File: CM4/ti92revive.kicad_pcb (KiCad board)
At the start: 2 copper layers, 205 x 116.7 mm, 175 parts, among them J1 USB_B, J2 Conn_01x02, J3 Conn_01x02, J4 USB_A, J5 USB_A, Q1 EMH3, U1 Compute_Module_4_Connectors, U2 NCP114ASN330T1G, U3 BQ25887RGET, U4 MAX17643, U5 ATTINY85-20PU, U6 TQ2SA-L2-3V-Z-Remake, U7 TUSB4041I, U8 TLV740P, U9 SK5126, Y1 24 MHz

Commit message: Cleaned Up the Matrix contolller
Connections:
- net FB renamed /PowerSupply/FB
- U9 pad 49: (no net) -> GND

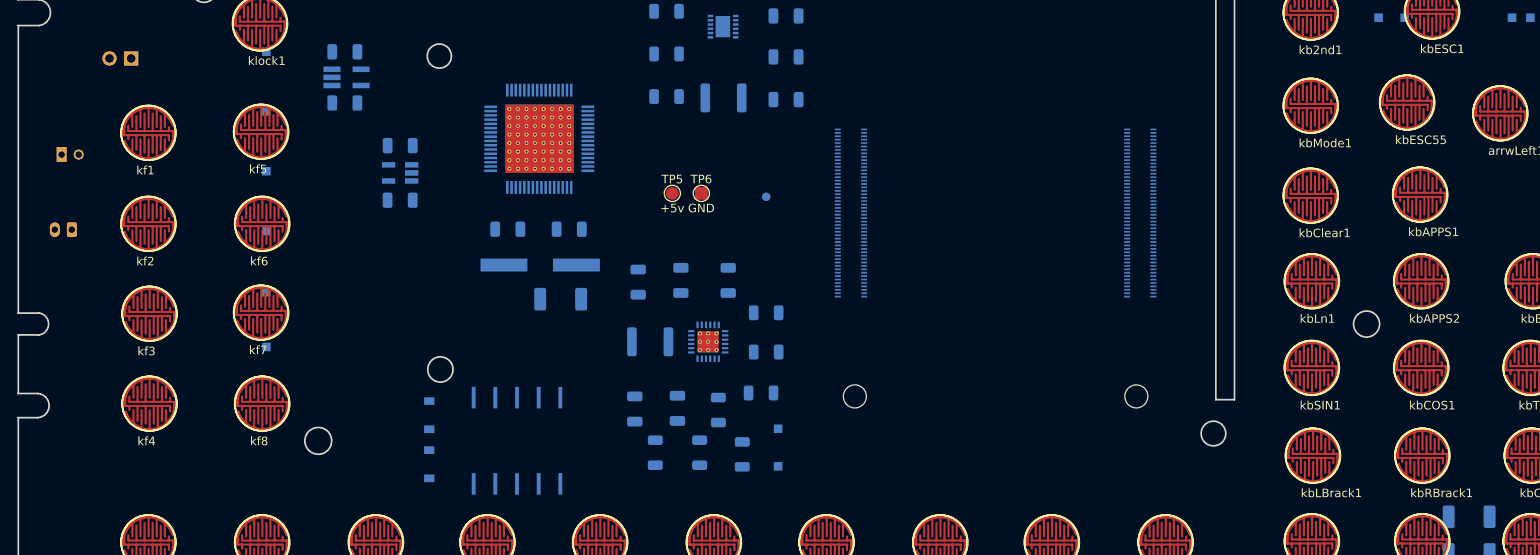
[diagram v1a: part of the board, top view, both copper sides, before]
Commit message: added battery connecoectors and emmcbootdisable jumpper
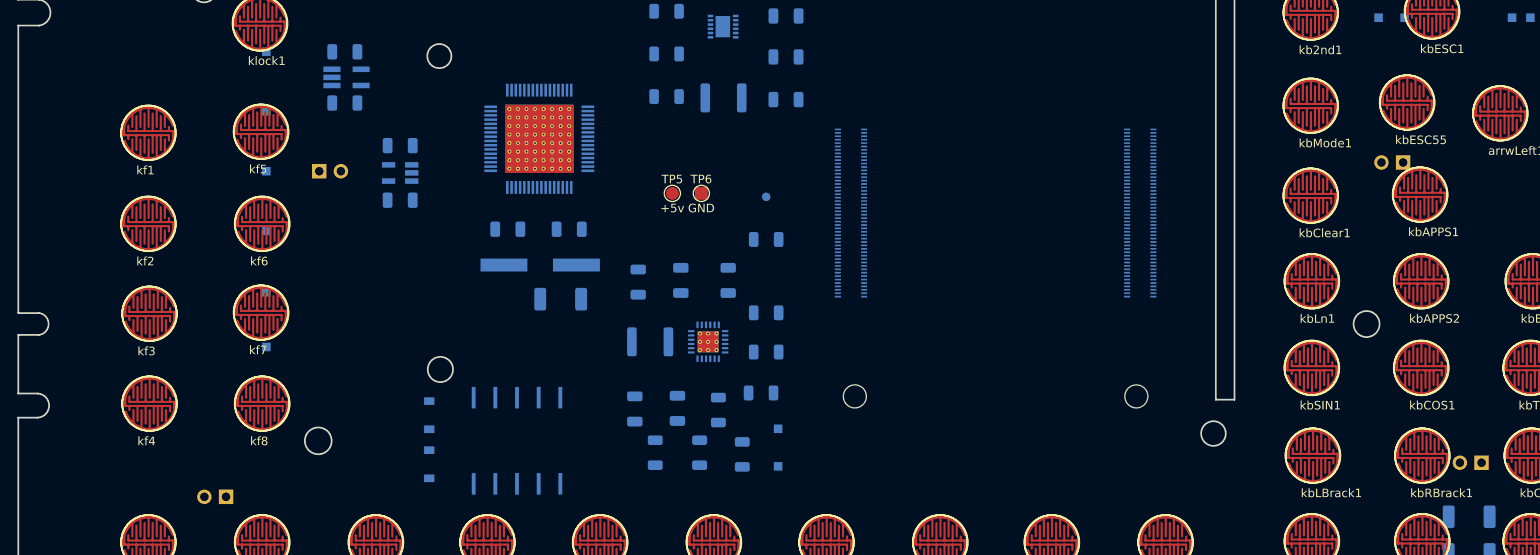
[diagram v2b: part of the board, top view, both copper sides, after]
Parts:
- added JP4: nRPIBOOT, Connector_PinHeader_2.54mm:PinHeader_1x02_P2.54mm_Horizontal, B.Cu at (215.1, 66.2)
- added R19: 300, Resistor_SMD:R_1206_3216Metric, B.Cu at (140.4, 75.2)
- J2: value Conn_01x02 -> Bat0; footprint Connector_JST:JST_PH_B2B-PH-K_1x02_P2.00mm_Vertical -> Connector_PinHeader_2.54mm:PinHeader_1x02_P2.54mm_Horizontal
- J3: value Conn_01x02 -> Bat1; footprint Connector_JST:JST_PH_B2B-PH-K_1x02_P2.00mm_Vertical -> Connector_PinHeader_2.54mm:PinHeader_1x02_P2.54mm_Horizontal
- TH1: value 10K -> 10K Thermister; footprint Connector_PinSocket_2.54mm:PinSocket_1x02_P2.54mm_Vertical -> Connector_PinHeader_2.54mm:PinHeader_1x02_P2.54mm_Horizontal
- moved J3 167.5 mm to (224.3, 101.4), turned to 90 degrees
- moved J2 43.7 mm to (77.1, 105.4), turned to 90 degrees
- moved TH1 25.7 mm to (88.0, 67.2), turned to -90 degrees
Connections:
- U1 pad 93: unconnected-(U1-Pad93) -> Net-(U1-Pad93)

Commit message: Finally Added the display!!!!
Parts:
- added U10: 4inch_RPi_LCD_(C), Connector_PinSocket_2.54mm:PinSocket_2x13_P2.54mm_Vertical, F.Cu at (154.5, 83.3)
- moved U1 9.87 mm to (176.6, 68.8)
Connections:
- net GND renamed Earth_Clean
- U1 pad 28: unconnected-(U1-Pad28) -> TP_SO
- U1 pad 30: piWatchDogPin -> RST
- U1 pad 31: unconnected-(U1-Pad31) -> LCD_SI/TP_SI
- U1 pad 34: unconnected-(U1-Pad34) -> LCD_RS
- U1 pad 36: unconnected-(U1-Pad36) -> TP_IRQ
- U1 pad 38: unconnected-(U1-Pad38) -> TP_CS
- U1 pad 40: unconnected-(U1-Pad40) -> piWatchDogPin
- U1 pad 44: unconnected-(U1-Pad44) -> LCD_CS
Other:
- outline, holes or cut-outs redrawn

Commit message: Started the "fun" of routing
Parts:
- arrwDWN1, arrwLeft1, arrwRight1, arrwUP1, kN666, kb2nd1, kbA1, kbALT1, kbALTG1, kbAPPS1, kbAPPS2, kbAnex2, kbB1, kbBKSP1, kbC1, kbCOS1, kbClear1, kbComa1, kbD1, kbDiv1, kbDot1, kbDot2, kbENT1, kbESC1, kbESC55, kbEnterNum1, kbEnterNum66, kbF1, kbG1, kbH1, kbI1, kbJ1, kbK1, kbL1, kbLBrack1, kbLn1, kbM1, kbMinus1, kbMode1, kbMult1, kbN1, kbN2, kbN3, kbN4, kbN5, kbN521, kbN6, kbN7, kbN8, kbN9, kbNeg1, kbO1, kbP1, kbPI1, kbPLUS1, kbPowerButton1, kbQ1, kbR1, kbRBrack1, kbRET1, kbRET32, kbS1, kbSIN1, kbShiftL1, kbSpace1, kbSpace2, kbT1, kbTAB1, kbTAN1, kbU1, kbV1, kbW1, kbX1, kbY1, kbZ1, kf1, kf2, kf3, kf4, kf5, kf6, kf7, kf8, klock1, kwE1: footprint 18650:Kbpad -> lib:Kbpad
- moved J2 194.1 mm to (271.1, 99.6)
- moved TH1 184.6 mm to (268.1, 107.6)
- moved TP21 92.4 mm to (123.6, 61.0), turned to -90 degrees
- moved TP20 89.7 mm to (123.6, 63.0), turned to -90 degrees
- moved TP13 75.0 mm to (153.2, 65.0), turned to 90 degrees
- moved TP19 74.9 mm to (153.2, 75.8), turned to 90 degrees
- moved TP22 72.8 mm to (153.2, 67.2), turned to 90 degrees
- moved TP17 72.7 mm to (153.2, 73.8), turned to 90 degrees
- moved TP16 71.6 mm to (153.2, 69.4), turned to 90 degrees
- moved TP18 71.5 mm to (153.2, 71.6), turned to 90 degrees
- moved J3 56.8 mm to (281.1, 100.2)
- moved JP4 54.4 mm to (173.8, 101.6), turned to 0 degrees
- moved TP23 12.4 mm to (126.2, 117.4), turned to 0 degrees
- moved TP24 10.8 mm to (137.8, 117.4), turned to 0 degrees
- moved C14 7.71 mm to (109.6, 74.0)
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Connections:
- net Net-(TP12-Pad1) renamed usbOTG_ID
- net SerialPin14 renamed LCD_SCK/TP_SCK
- U10 pad 10: (no net) -> unconnected-(U10-Pad10)
- U10 pad 12: (no net) -> unconnected-(U10-Pad12)
- U10 pad 13: (no net) -> unconnected-(U10-Pad13)
- U10 pad 14: (no net) -> Earth_Clean
- U10 pad 15: (no net) -> unconnected-(U10-Pad15)
- U10 pad 16: (no net) -> unconnected-(U10-Pad16)
- U10 pad 17: (no net) -> +3.3 High Current
- U10 pad 20: (no net) -> Earth_Clean
- U10 pad 25: (no net) -> Earth_Clean
- U10 pad 3: (no net) -> unconnected-(U10-Pad3)
- U10 pad 4: (no net) -> +5
- U10 pad 5: (no net) -> unconnected-(U10-Pad5)
- U10 pad 7: (no net) -> unconnected-(U10-Pad7)
- U10 pad 8: (no net) -> unconnected-(U10-Pad8)
- U10 pad 9: (no net) -> Earth_Clean
- U9 pad 10: col1 -> row1
- U9 pad 27: col1 -> col2
- U9 pad 28: col1 -> col3
- U9 pad 29: col1 -> col4
- U9 pad 30: col1 -> col5
- U9 pad 31: col1 -> col6
- U9 pad 8: col1 -> row3
- U9 pad 9: col1 -> col5
- arrwLeft1 pad 1: col1 -> col6
- kbA1 pad 2: col1 -> col5
- kbALT1 pad 1: col1 -> col2
- kbALTG1 pad 1: col1 -> col4
- kbAPPS1 pad 1: col1 -> col5
- kbAPPS2 pad 1: col1 -> col5
- kbB1 pad 1: col1 -> col5
- kbB1 pad 2: col1 -> row3
- kbBKSP1 pad 2: col1 -> col5
- kbC1 pad 1: col1 -> col3
- kbC1 pad 2: col1 -> row3
- kbClear1 pad 1: col1 -> col3
- kbComa1 pad 1: col1 -> col3
- kbD1 pad 1: col1 -> col2
- kbD1 pad 2: col1 -> col5
- kbDiv1 pad 1: col1 -> col4
- kbDot1 pad 1: col1 -> col5
- kbDot2 pad 2: col1 -> row3
- kbEnterNum1 pad 1: col1 -> col6
- kbEnterNum66 pad 1: col1 -> col6
- kbF1 pad 1: col1 -> col3
- kbF1 pad 2: col1 -> col5
- kbG1 pad 1: col1 -> col4
- kbG1 pad 2: col1 -> col5
- kbH1 pad 1: col1 -> col5
- kbH1 pad 2: col1 -> col5
- kbI1 pad 2: col1 -> row1
- kbJ1 pad 1: col1 -> col6
- kbJ1 pad 2: col1 -> col5
- kbK1 pad 2: col1 -> col5
- kbL1 pad 2: col1 -> col5
- kbLn1 pad 1: col1 -> col4
- kbM1 pad 2: col1 -> row3
- kbMode1 pad 1: col1 -> col2
- kbN3 pad 1: col1 -> col2
- kbN4 pad 1: col1 -> col4
- kbN5 pad 1: col1 -> col5
- kbN521 pad 1: col1 -> col5
- kbN6 pad 1: col1 -> col6
- kbN6 pad 2: col1 -> row3
- kbN7 pad 1: col1 -> col6
- kbNeg1 pad 1: col1 -> col6
- kbO1 pad 2: col1 -> row1
- kbP1 pad 2: col1 -> row1
- kbPLUS1 pad 1: col1 -> col3
- kbQ1 pad 2: col1 -> row1
- kbR1 pad 1: col1 -> col3
- kbR1 pad 2: col1 -> row1
- kbRBrack1 pad 1: col1 -> col2
- kbRET1 pad 2: col1 -> row3
- kbRET32 pad 2: col1 -> row3
- kbS1 pad 2: col1 -> col5
- kbSpace1 pad 1: col1 -> col3
- kbSpace2 pad 1: col1 -> col3
- kbT1 pad 1: col1 -> col4
- kbT1 pad 2: col1 -> row1
- kbTAB1 pad 2: col1 -> row3
- kbU1 pad 1: col1 -> col6
- kbU1 pad 2: col1 -> row1
- kbV1 pad 1: col1 -> col4
- kbV1 pad 2: col1 -> row3
- kbW1 pad 2: col1 -> row1
- kbX1 pad 1: col1 -> col2
- kbX1 pad 2: col1 -> row3
- kbY1 pad 1: col1 -> col5
- kbY1 pad 2: col1 -> row1
- kbZ1 pad 2: col1 -> row3
- kf2 pad 1: col1 -> col2
- kf3 pad 1: col1 -> col3
- kf4 pad 1: col1 -> col4
- kf5 pad 1: col1 -> col5
- kf6 pad 1: col1 -> col6
- kwE1 pad 1: col1 -> col2
- kwE1 pad 2: col1 -> row1
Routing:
- net row1: track 0.00 -> 206.7 mm, vias 0 -> 3
- net row0: track 0.00 -> 148.7 mm, vias 0 -> 1
- net col0: track 0.00 -> 130.3 mm, vias 0 -> 2
- net col1: track 0.00 -> 111.3 mm
- net Earth_Clean: track 0.00 -> 69.8 mm, vias 0 -> 2
- net +5: track 0.00 -> 49.0 mm, vias 0 -> 4
- net Net-(C10-Pad2): track 0.00 -> 25.8 mm, vias 0 -> 5
- net Net-(C9-Pad1): track 0.00 -> 22.6 mm, vias 0 -> 2
- net Net-(C1-Pad2): track 0.00 -> 20.8 mm
- net Net-(JP3-Pad2): track 0.00 -> 19.9 mm
- net Net-(JP2-Pad1): track 0.00 -> 19.5 mm, vias 0 -> 2
- net Net-(R1-Pad2): track 0.00 -> 18.1 mm, vias 0 -> 2
- net Net-(C3-Pad1): track 0.00 -> 15.6 mm, vias 0 -> 2
- net Net-(C2-Pad1): track 0.00 -> 12.1 mm
- net Net-(R4-Pad2): track 0.00 -> 12.0 mm, vias 0 -> 2
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
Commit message: i hate routing
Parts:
- moved Q1 43.8 mm to (149.0, 89.8)
- moved U5 43.8 mm to (161.3, 93.8)
- moved JP1 43.8 mm to (155.5, 89.6)
- moved R12 43.8 mm to (148.9, 95.0)
- moved R13 43.8 mm to (148.9, 100.2)
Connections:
- U9 pad 9: col5 -> row2
- kbA1 pad 2: col5 -> row2
- kbBKSP1 pad 2: col5 -> row2
- kbD1 pad 2: col5 -> row2
- kbF1 pad 2: col5 -> row2
- kbG1 pad 2: col5 -> row2
- kbH1 pad 2: col5 -> row2
- kbJ1 pad 2: col5 -> row2
- kbK1 pad 2: col5 -> row2
- kbL1 pad 2: col5 -> row2
- kbS1 pad 2: col5 -> row2
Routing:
- net col3: track 0.00 -> 382.4 mm, vias 0 -> 8
- net col4: track 0.00 -> 364.0 mm, vias 0 -> 9
- net col2: track 0.00 -> 337.6 mm, vias 0 -> 6
- net col6: track 0.00 -> 336.2 mm, vias 0 -> 5
- net row2: track 0.00 -> 134.4 mm, vias 0 -> 5
- net col1: track 111.3 -> 115.4 mm
- net col5: track 0.00 -> 2.64 mm
- net col0: track 130.3 -> 131.9 mm

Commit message: Heck Routing
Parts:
- moved R15 150.7 mm to (98.2, 31.9)
- moved R16 150.7 mm to (98.2, 22.9)
- moved R17 150.7 mm to (98.2, 27.3)
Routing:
- net col7: track 0.00 -> 422.4 mm, vias 0 -> 14
- net col8: track 0.00 -> 359.9 mm, vias 0 -> 11
- net row4: track 0.00 -> 346.3 mm, vias 0 -> 9
- net col1: track 115.4 -> 177.5 mm, vias 0 -> 3
- net col4: track 364.0 -> 359.2 mm
- net row1: track 206.7 -> 211.4 mm
- net col2: track 337.6 -> 340.4 mm
- net row0: track 148.7 -> 151.4 mm
- net col6: track 336.2 -> 334.6 mm
- net col3: track 382.4 -> 381.1 mm
- net Net-(JP2-Pad1): track 19.5 -> 18.2 mm

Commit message: Wow, This is kinda fun
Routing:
- net row5: track 0.00 -> 295.1 mm, vias 0 -> 17
- net col1: track 177.5 -> 359.2 mm, vias 3 -> 10
- net col4: track 359.2 -> 362.0 mm
- net col8: track 359.9 -> 358.0 mm
- net col2: track 340.4 -> 341.7 mm
- net col6: track 334.6 -> 335.8 mm
- net col3: track 381.1 -> 382.0 mm

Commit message: More wires hehehehe
wow so good
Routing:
- net col5: track 2.64 -> 344.0 mm, vias 0 -> 20
- net row7: track 0.00 -> 228.4 mm, vias 0 -> 9
- net row6: track 0.00 -> 198.8 mm, vias 0 -> 10
- net row3: track 0.00 -> 189.2 mm, vias 0 -> 12
- net row2: track 134.3 -> 69.6 mm, vias 5 -> 3
- net col2: track 341.7 -> 346.2 mm
- net col8: track 358.0 -> 361.5 mm
- net col6: track 335.8 -> 339.0 mm
- net col4: track 362.0 -> 365.1 mm
- net row4: track 346.3 -> 344.0 mm
- net col7: track 422.2 -> 423.1 mm
- net col1: track 359.2 -> 358.6 mm
